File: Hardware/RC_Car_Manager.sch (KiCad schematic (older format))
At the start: 32 parts, among them P1 7.4V BATTERY_IN, P2 ULTRASONIC, P3 RIHGT_IR, P4 LEFT_IR, P5 7.4V BATTERY_OUT, P6 ESC, P7 SERVO, Q1 2N3904, Q2 FQP48P06, SW1 SPST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

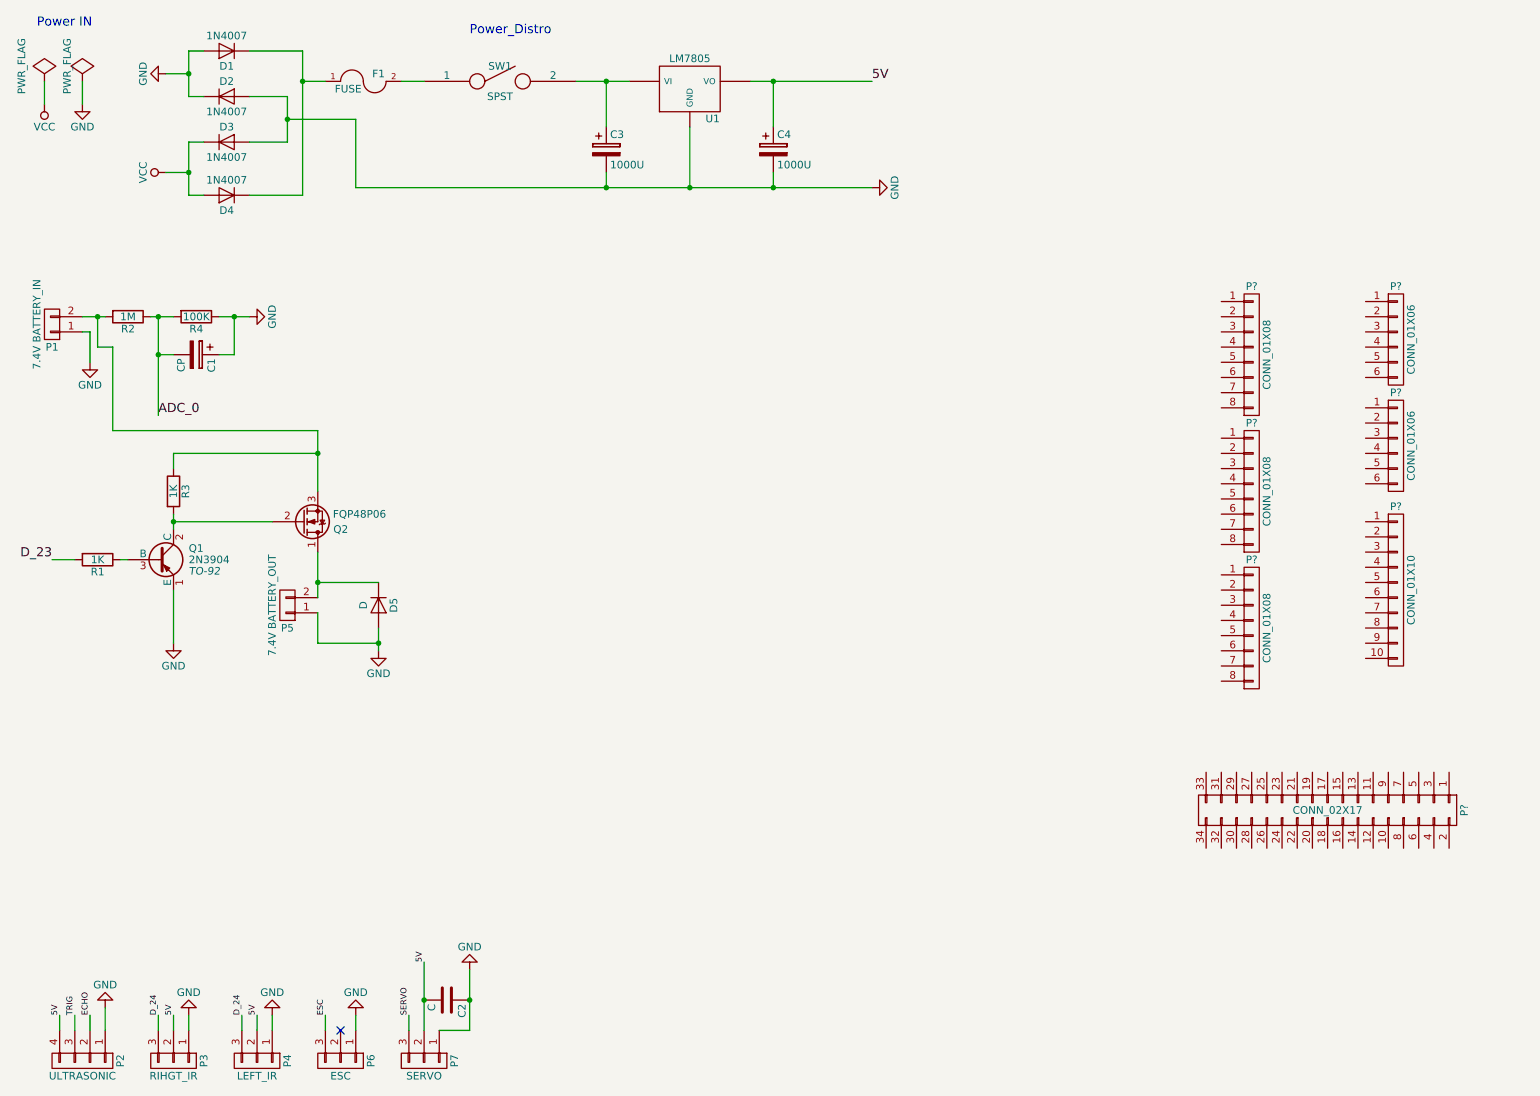
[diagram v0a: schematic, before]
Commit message: Orgnise and update schematics
This includes transfering each component to it's own schematic [file]
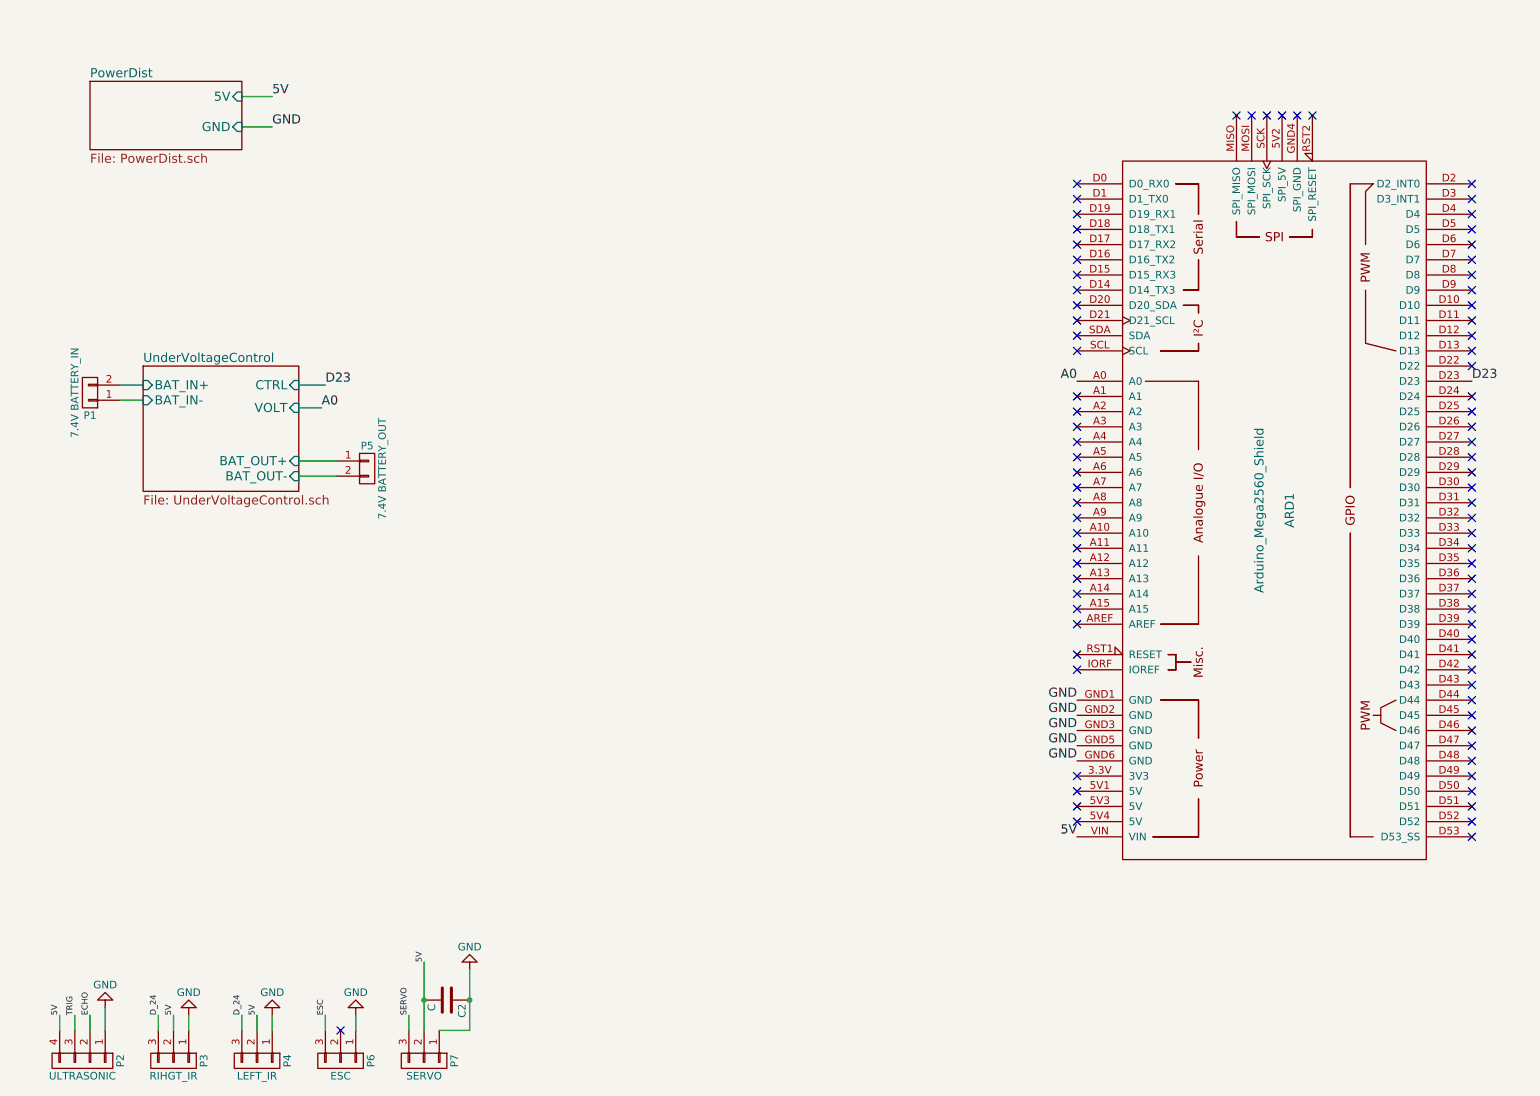
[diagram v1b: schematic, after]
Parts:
- removed C1: CP, symbol CP
- removed C3, C4: 1000U, symbol CP
- removed D1, D2, D3, D4: 1N4007, symbol D
- removed D5: D, symbol D
- removed F1: FUSE, symbol FUSE
- removed P? (x3): CONN_01X08, symbol CONN_01X08
- removed P? (x2): CONN_01X06, symbol CONN_01X06
- removed P?: CONN_01X10, symbol CONN_01X10
- removed P?: CONN_02X17, symbol CONN_02X17
- removed Q1: 2N3904, TO-92, symbol 2SA1016
- removed Q2: FQP48P06, symbol Q_NMOS_DGS
- removed R1, R3: 1K, symbol R
- removed R2: 1M, symbol R
- removed R4: 100K, symbol R
- removed SW1: SPST, symbol SPST
- removed U1: LM7805, symbol LM7805
- added ARD1: Arduino_Mega2560_Shield, symbol Arduino_Mega2560_Shield
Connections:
- net 5V: now also ARD1.VIN
- net GND: now also ARD1.GND1 (GND), ARD1.GND2 (GND), ARD1.GND3 (GND), ARD1.GND5 (GND), ARD1.GND6 (GND); no longer P1.1 (P1), P5.1 (P1)
- net UnderVoltageControl/BAT_IN+: now reaches P1.2 (P2)
- net UnderVoltageControl/BAT_OUT-: now reaches P5.2 (P2)
- new net A0: ARD1.A0
- new net D23: ARD1.D23
- new net UnderVoltageControl/BAT_IN-: P1.1 (P1)
- new net UnderVoltageControl/BAT_OUT+: P5.1 (P1)
- no-connect marks 1 -> 84
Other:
- note removed: "Power IN"
- note removed: "Power_Distro"
- moved on the sheet: P1, P5

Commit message: Add receiver component
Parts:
- added REC1: Receiver, symbol Receiver
- renumbered C2 to C1, P2 to P1, P1 to P2, P6 to P5, P5 to P6
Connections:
- net 5V: now also REC1.7 (V_in)
- net GND: now also REC1.8 (GND)
- net A10: now reaches ARD1.A10
- net A10: now also REC1.3 (CH3)
- net A11: now reaches ARD1.A11
- net A11: now also REC1.4 (CH4)
- net A12: now reaches ARD1.A12
- net A12: now also REC1.5 (CH5)
- net A13: now reaches ARD1.A13
- net A13: now also REC1.6 (CH6)
- net A8: now reaches ARD1.A8
- net A8: now also REC1.1 (CH1)
- net A9: now reaches ARD1.A9
- net A9: now also REC1.2 (CH2)
- no-connect marks 84 -> 78
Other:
- moved on the sheet: P2, P6
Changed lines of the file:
@@
 LIBS:valves
 LIBS:arduino
-LIBS:RC_Car_Manager-cache
+LIBS:RC_CAR
 EELAYER 25 0
 EELAYER END
@@
 $EndDescr
 $Comp
-L CONN_01X02 P1
+L CONN_01X02 P2
 U 1 1 576D1902
-P 1100 3000
-F 0 "P1" H 1100 3150 50  0000 C CNN
-F 1 "7.4V BATTERY_IN" V 1200 3000 50  0000 C CNN
-F 2 "" H 1100 3000 50  0000 C CNN
-F 3 "" H 1100 3000 50  0000 C CNN
-	1    1100 3000
-	-1   0    0    1
-$EndComp
-$Comp
-L CONN_01X02 P5
+P 3550 1200
+F 0 "P2" H 3550 1350 50  0000 C CNN
+F 1 "7.4V BATTERY_IN" V 3650 1200 50  0000 C CNN
+F 2 "" H 3550 1200 50  0000 C CNN
+F 3 "" H 3550 1200 50  0000 C CNN
+	1    3550 1200
+	-1   0    0    1
+$EndComp
+$Comp
+L CONN_01X02 P6
 U 1 1 576D31E2
-P 2925 3500
-F 0 "P5" H 2925 3650 50  0000 C CNN
-F 1 "7.4V BATTERY_OUT" V 3025 3500 50  0000 C CNN
-F 2 "" H 2925 3500 50  0000 C CNN
-F 3 "" H 2925 3500 50  0000 C CNN
-	1    2925 3500
+P 5375 1700
+F 0 "P6" H 5375 1850 50  0000 C CNN
+F 1 "7.4V BATTERY_OUT" V 5475 1700 50  0000 C CNN
+F 2 "" H 5375 1700 50  0000 C CNN
+F 3 "" H 5375 1700 50  0000 C CNN
+	1    5375 1700
 	1    0    0    -1
 $EndComp
 $Comp
-L CONN_01X04 P2
+L CONN_01X04 P1
 U 1 1 576D41F2
 P 1050 7400
-F 0 "P2" H 1050 7650 50  0000 C CNN
+F 0 "P1" H 1050 7650 50  0000 C CNN
 F 1 "ULTRASONIC" V 1150 7400 50  0000 C CNN
 F 2 "" H 1050 7400 50  0000 C CNN
@@
 $EndComp
 $Comp
-L CONN_01X03 P6
+L CONN_01X03 P5
 U 1 1 576D42FD
 P 2750 7400
-F 0 "P6" H 2750 7600 50  0000 C CNN
+F 0 "P5" H 2750 7600 50  0000 C CNN
 F 1 "ESC" V 2850 7400 50  0000 C CNN
 F 2 "" H 2750 7400 50  0000 C CNN
@@
 $EndComp
 $Comp
-L C C2
+L C C1
 U 1 1 576D43B4
 P 3450 7000
-F 0 "C2" H 3475 7100 50  0000 L CNN
+F 0 "C1" H 3475 7100 50  0000 L CNN
 F 1 "C" H 3475 6900 50  0000 L CNN
 F 2 "" H 3488 6850 50  0000 C CNN
@@
 	1100 7100 1100 7200
 $Comp
-L GND #PWR2
+L GND #PWR1
 U 1 1 576D5A6C
 P 1200 7050
-F 0 "#PWR2" H 1200 6800 50  0001 C CNN
+F 0 "#PWR1" H 1200 6800 50  0001 C CNN
 F 1 "GND" H 1200 6900 50  0000 C CNN
 F 2 "" H 1200 7050 50  0000 C CNN
@@
 	1550 7100 1550 7200
 $Comp
-L GND #PWR4
+L GND #PWR2
 U 1 1 576D5C22
 P 1750 7100
-F 0 "#PWR4" H 1750 6850 50  0001 C CNN
+F 0 "#PWR2" H 1750 6850 50  0001 C CNN
 F 1 "GND" H 1750 6950 50  0000 C CNN
 F 2 "" H 1750 7100 50  0000 C CNN
@@
 	2100 7100 2100 7200
 $Comp
-L GND #PWR6
+L GND #PWR3
 U 1 1 576D5DA2
 P 2300 7100
-F 0 "#PWR6" H 2300 6850 50  0001 C CNN
+F 0 "#PWR3" H 2300 6850 50  0001 C CNN
 F 1 "GND" H 2300 6950 50  0000 C CNN
 F 2 "" H 2300 7100 50  0000 C CNN
@@
 	2650 7100 2650 7200
 $Comp
-L GND #PWR7
+L GND #PWR4
 U 1 1 576D5F8C
 P 2850 7100
-F 0 "#PWR7" H 2850 6850 50  0001 C CNN
+F 0 "#PWR4" H 2850 6850 50  0001 C CNN
 F 1 "GND" H 2850 6950 50  0000 C CNN
 F 2 "" H 2850 7100 50  0000 C CNN
@@
 	3200 7100 3200 7200
 $Comp
-L GND #PWR9
+L GND #PWR5
 U 1 1 576D627D
 P 3600 6800
-F 0 "#PWR9" H 3600 6550 50  0001 C CNN
+F 0 "#PWR5" H 3600 6550 50  0001 C CNN
 F 1 "GND" H 3600 6650 50  0000 C CNN
 F 2 "" H 3600 6800 50  0000 C CNN
@@
 $EndComp
 $Sheet
-S 1100 950  1000 450
+S 1125 1175 1000 450
 U 5A340F55
 F0 "PowerDist" 60
 F1 "PowerDist.sch" 60
-F2 "5V" I R 2100 1050 60
-F3 "GND" I R 2100 1250 60
+F2 "5V" I R 2125 1275 60
+F3 "GND" I R 2125 1475 60
 $EndSheet
-Text Label 2300 1250 0    60   ~ 0
-GND
-Wire Wire Line
-	2300 1250 2100 1250
-Text Label 2300 1050 0    60   ~ 0
-5V
-Wire Wire Line
-	2300 1050 2100 1050
+Text Label 2325 1475 0    60   ~ 0
+GND
+Wire Wire Line
+	2325 1475 2125 1475
+Text Label 2325 1275 0    60   ~ 0
+5V
+Wire Wire Line
+	2325 1275 2125 1275
 NoConn ~ 8650 1175
 NoConn ~ 8750 1175
@@
 NoConn ~ 7600 4425
 NoConn ~ 7600 4325
-NoConn ~ 7600 4225
-NoConn ~ 7600 4125
-NoConn ~ 7600 4025
-NoConn ~ 7600 3925
-NoConn ~ 7600 3825
-NoConn ~ 7600 3725
 NoConn ~ 7600 3625
 NoConn ~ 7600 3525
@@
 NoConn ~ 7600 1625
 $Sheet
-S 1450 2825 1025 825
+S 3900 1025 1025 825
 U 5A34C92E
 F0 "UnderVoltageControl" 60
 F1 "UnderVoltageControl.sch" 60
-F2 "BAT_IN+" I L 1450 2950 60
-F3 "BAT_IN-" I L 1450 3050 60
-F4 "BAT_OUT+" I R 2475 3450 60
-F5 "BAT_OUT-" I R 2475 3550 60
-F6 "CTRL" I R 2475 2950 60
-F7 "VOLT" I R 2475 3100 60
+F2 "BAT_IN+" I L 3900 1150 60
+F3 "BAT_IN-" I L 3900 1250 60
+F4 "BAT_OUT+" I R 4925 1650 60
+F5 "BAT_OUT-" I R 4925 1750 60
+F6 "CTRL" I R 4925 1150 60
+F7 "VOLT" I R 4925 1300 60
 $EndSheet
 Wire Wire Line
-	2475 3550 2725 3550
-Wire Wire Line
-	2725 3450 2475 3450
-Wire Wire Line
-	1450 2950 1300 2950
-Wire Wire Line
-	1450 3050 1300 3050
-Text Label 2625 3100 0    60   ~ 0
+	4925 1750 5175 1750
+Wire Wire Line
+	5175 1650 4925 1650
+Wire Wire Line
+	3900 1150 3750 1150
+Wire Wire Line
+	3900 1250 3750 1250
+Text Label 5075 1300 0    60   ~ 0
 A0
 Wire Wire Line
-	2625 3100 2475 3100
-Text Label 2650 2950 0    60   ~ 0
+	5075 1300 4925 1300
+Text Label 5100 1150 0    60   ~ 0
 D23
 Wire Wire Line
-	2650 2950 2475 2950
+	5100 1150 4925 1150
 Text Label 10200 2925 0    60   ~ 0
 D23
 Text Label 7600 2925 2    60   ~ 0
 A0
+$Comp
+L Receiver REC1
+U 1 1 5A353D45
+P 1575 3750
+F 0 "REC1" H 2575 3800 60  0000 C CNN
+F 1 "Receiver" H 1775 4250 60  0000 C CNN
+F 2 "" H 1575 3750 60  0001 C CNN
+F 3 "" H 1575 3750 60  0001 C CNN
+	1    1575 3750
+	1    0    0    -1
+$EndComp
+Text Label 1375 3400 2    60   ~ 0
+5V
+Text Label 1375 3500 2    60   ~ 0
+GND
+Text Label 1825 3950 3    60   ~ 0
+A8
+Text Label 7600 3725 2    60   ~ 0
+A8
+Text Label 1925 3950 3    60   ~ 0
+A9
+Text Label 7600 3825 2    60   ~ 0
+A9
+Text Label 2025 3950 3    60   ~ 0
+A10
+Text Label 7600 3925 2    60   ~ 0
+A10
+Text Label 2125 3950 3    60   ~ 0
+A11
+Text Label 7600 4025 2    60   ~ 0
+A11
+Text Label 2225 3950 3    60   ~ 0
+A12
+Text Label 7600 4125 2    60   ~ 0
+A12
+Text Label 2325 3950 3    60   ~ 0
+A13
+Text Label 7600 4225 2    60   ~ 0
+A13
 $EndSCHEMATC

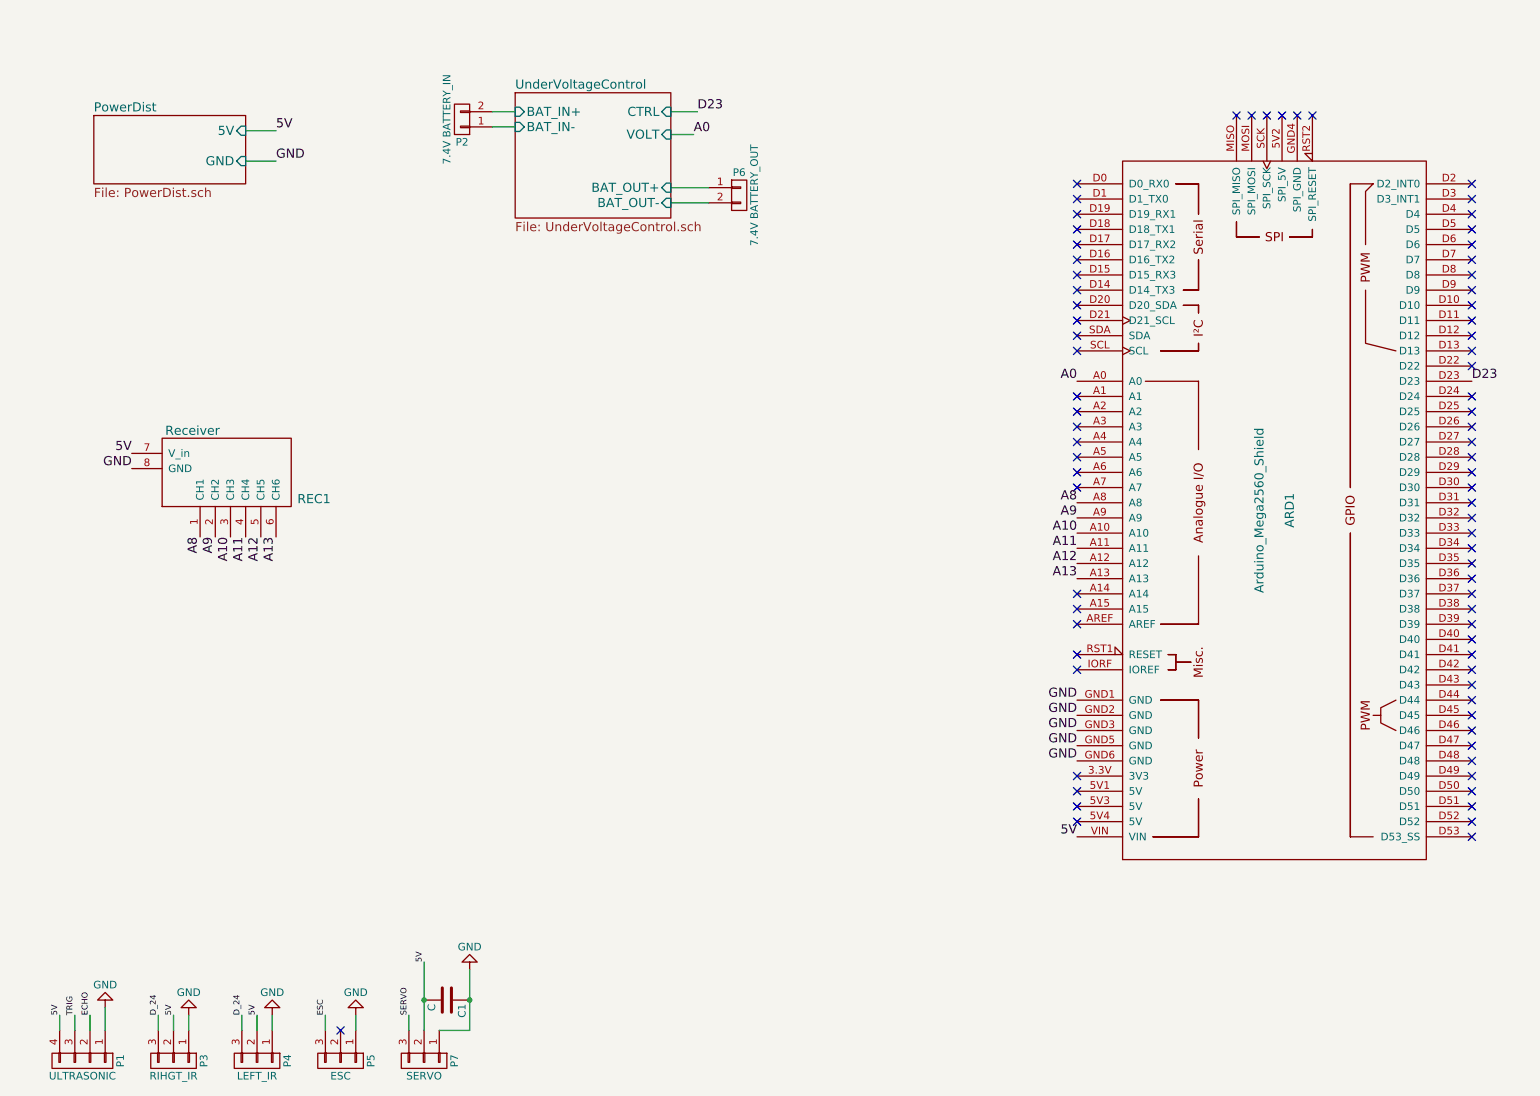
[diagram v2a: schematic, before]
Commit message: Resolves 2N3904 transistor miss match
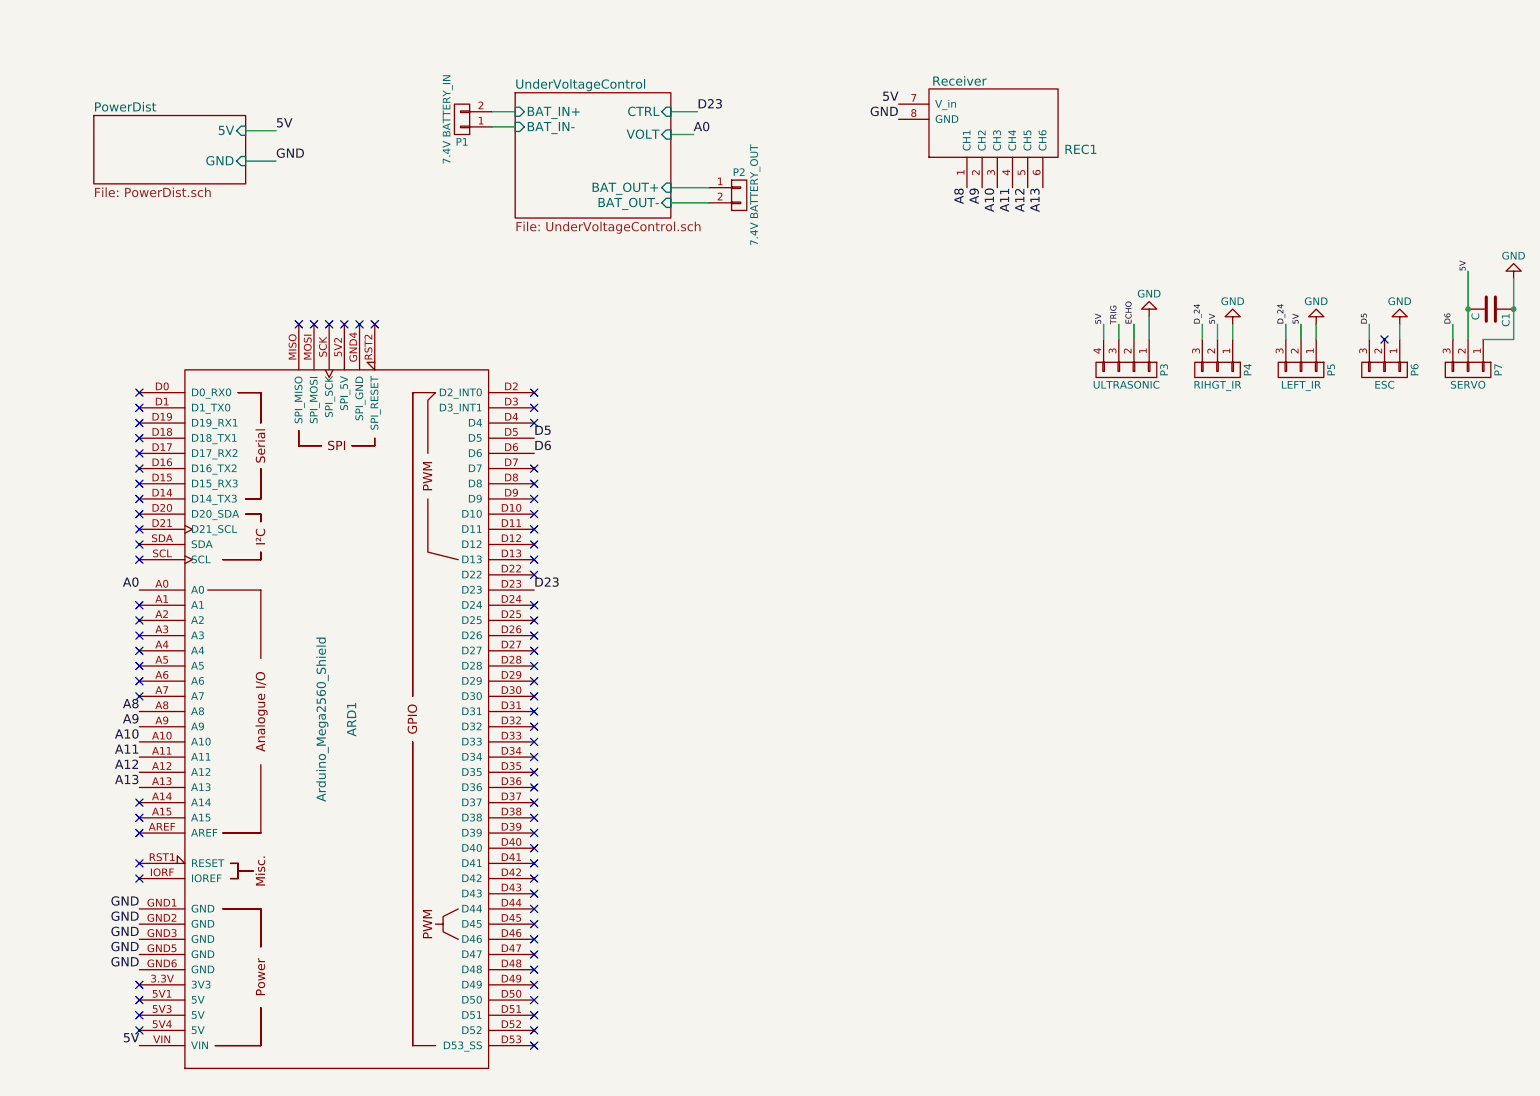
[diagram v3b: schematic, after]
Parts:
- renumbered P2 to P1, P6 to P2, P1 to P3, P3 to P4, P4 to P5, P5 to P6
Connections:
- net ESC is gone; now on net D5: P6.3 (P3)
- net SERVO is gone; now on net D6: P7.3 (P3)
- net D5: now reaches ARD1.D5
- net D6: now reaches ARD1.D6
- no-connect marks 78 -> 76
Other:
- moved on the sheet: ARD1, C1, P3, P4, P5, P6, P7, REC1
